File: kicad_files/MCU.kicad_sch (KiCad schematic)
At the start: 24 parts, among them SW1 SW_Push, SW2 SW_Push, U1 STM32F407VGTx, Y1 LFXTAL036869Reel 8MHz Crystal

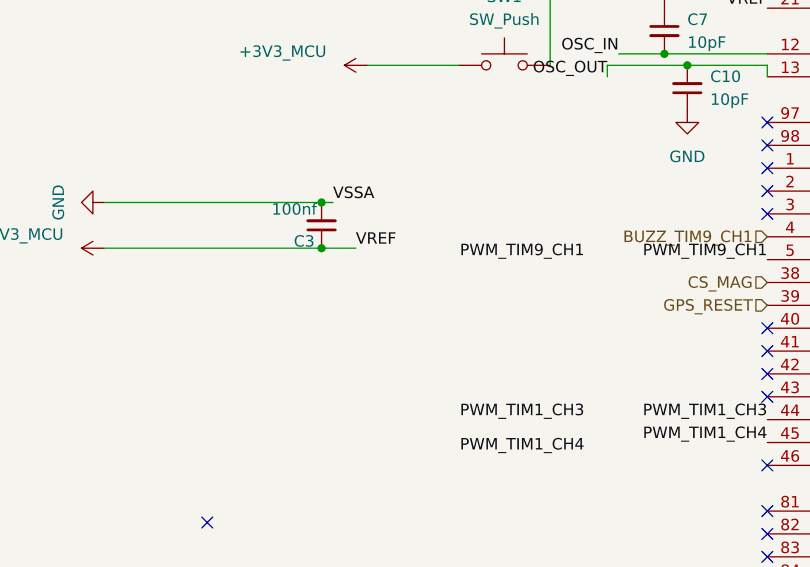
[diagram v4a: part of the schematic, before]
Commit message: add pwm tht hole
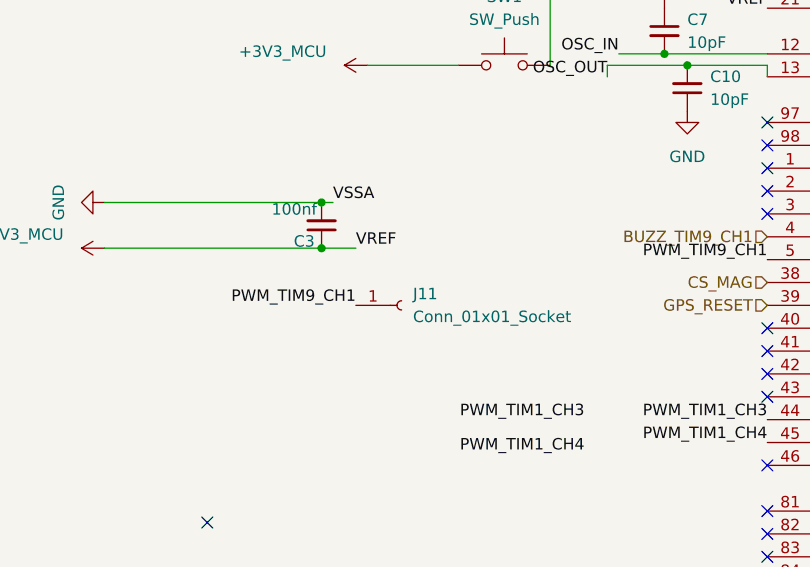
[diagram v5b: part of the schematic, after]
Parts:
- added J11: Conn_01x01_Socket, Connector_Wire:SolderWire-0.5sqmm_1x01_D0.9mm_OD2.1mm, symbol Connector:Conn_01x01_Socket
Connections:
- net PWM_TIM9_CH1: now also J11.1 (Pin_1)
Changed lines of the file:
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@@
 	)
 	(label "PWM_TIM9_CH1"
-		(at 179.07 132.08 180)
+		(at 153.67 137.16 180)
 		(effects
 			(font
@@
 					(unit 1)
 				)
+			)
+		)
+	)
+	(symbol
+		(lib_id "Connector:Conn_01x01_Socket")
+		(at 158.75 137.16 0)
+		(unit 1)
+		(body_style 1)
+		(exclude_from_sim no)
+		(in_bom yes)
+		(on_board yes)
+		(in_pos_files yes)
+		(dnp no)
+		(fields_autoplaced yes)
+		(property "Reference" "J11"
+			(at 160.02 135.8899 0)
+			(show_name no)
+			(do_not_autoplace no)
+			(effects
+				(font
+					(size 1.27 1.27)
+				)
+				(justify left)
+			)
+		)
+		(property "Value" "Conn_01x01_Socket"
+			(at 160.02 138.4299 0)
+			(show_name no)
+			(do_not_autoplace no)
+			(effects
+				(font
+					(size 1.27 1.27)
+				)
+				(justify left)
+			)
+		)
+		(property "Footprint" "Connector_Wire:SolderWire-0.5sqmm_1x01_D0.9mm_OD2.1mm"
+			(at 158.75 137.16 0)
+			(hide yes)
+			(show_name no)
+			(do_not_autoplace no)
+			(effects
+				(font
+					(size 1.27 1.27)
+				)
+			)
+		)
+		(property "Datasheet" ""
+			(at 158.75 137.16 0)
+			(hide yes)
+			(show_name no)
+			(do_not_autoplace no)
+			(effects
+				(font
+					(size 1.27 1.27)
+				)
+			)
+		)
+		(property "Description" "Generic connector, single row, 01x01, script generated"
+			(at 158.75 137.16 0)
+			(hide yes)
+			(show_name no)
+			(do_not_autoplace no)
+			(effects
+				(font
+					(size 1.27 1.27)
+				)
+			)
+		)
+		(pin "1"
+		)
+		(instances
+			(project "versorlite"
+				(path "/1a230af0-0a74-48f7-8607-b087121dda49/a6e36be3-aff5-4566-a903-d81edfd88a96"
+					(reference "J11")
+					(unit 1)
+				)

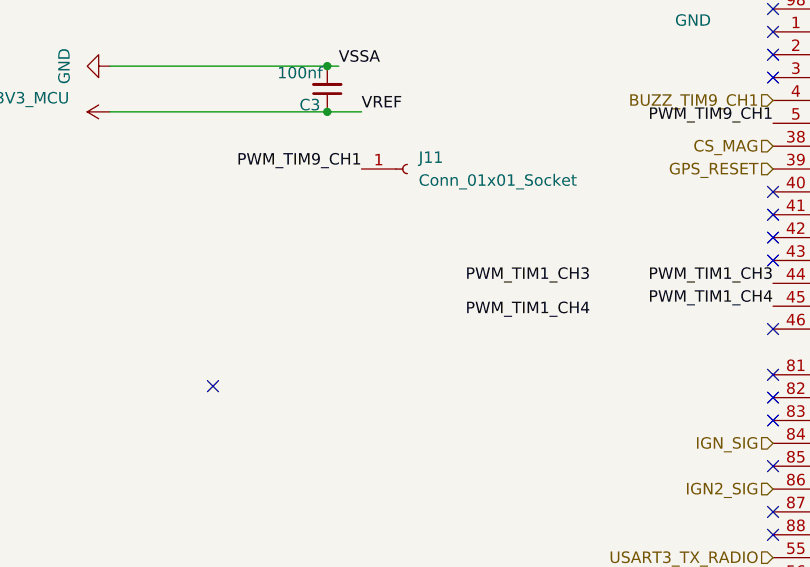
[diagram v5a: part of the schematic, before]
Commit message: add two more pwm holes
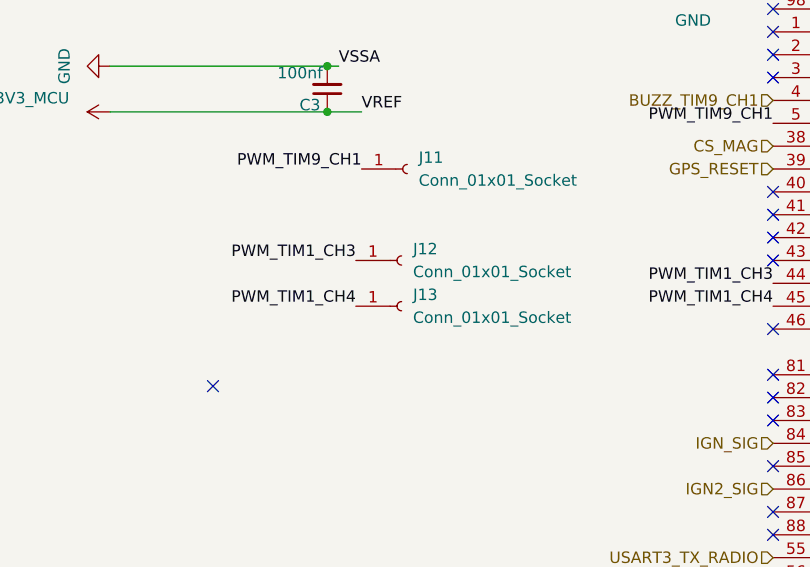
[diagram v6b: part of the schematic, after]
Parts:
- added J12, J13: Conn_01x01_Socket, Connector_Wire:SolderWire-0.5sqmm_1x01_D0.9mm_OD2.1mm, symbol Connector:Conn_01x01_Socket
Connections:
- net PWM_TIM1_CH3: now also J12.1 (Pin_1)
- net PWM_TIM1_CH4: now also J13.1 (Pin_1)
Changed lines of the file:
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@@
 	)
 	(label "PWM_TIM1_CH3"
-		(at 179.07 149.86 180)
+		(at 153.035 147.32 180)
 		(effects
 			(font
@@
 	)
 	(label "PWM_TIM1_CH4"
-		(at 179.07 153.67 180)
+		(at 153.035 152.4 180)
 		(effects
 			(font
@@
 	)
 	(symbol
+		(lib_id "Connector:Conn_01x01_Socket")
+		(at 158.115 152.4 0)
+		(unit 1)
+		(body_style 1)
+		(exclude_from_sim no)
+		(in_bom yes)
+		(on_board yes)
+		(in_pos_files yes)
+		(dnp no)
+		(fields_autoplaced yes)
+		(property "Reference" "J13"
+			(at 159.385 151.1299 0)
+			(show_name no)
+			(do_not_autoplace no)
+			(effects
+				(font
+					(size 1.27 1.27)
+				)
+				(justify left)
+			)
+		)
+		(property "Value" "Conn_01x01_Socket"
+			(at 159.385 153.6699 0)
+			(show_name no)
+			(do_not_autoplace no)
+			(effects
+				(font
+					(size 1.27 1.27)
+				)
+				(justify left)
+			)
+		)
+		(property "Footprint" "Connector_Wire:SolderWire-0.5sqmm_1x01_D0.9mm_OD2.1mm"
+			(at 158.115 152.4 0)
+			(hide yes)
+			(show_name no)
+			(do_not_autoplace no)
+			(effects
+				(font
+					(size 1.27 1.27)
+				)
+			)
+		)
+		(property "Datasheet" ""
+			(at 158.115 152.4 0)
+			(hide yes)
+			(show_name no)
+			(do_not_autoplace no)
+			(effects
+				(font
+					(size 1.27 1.27)
+				)
+			)
+		)
+		(property "Description" "Generic connector, single row, 01x01, script generated"
+			(at 158.115 152.4 0)
+			(hide yes)
+			(show_name no)
+			(do_not_autoplace no)
+			(effects
+				(font
+					(size 1.27 1.27)
+				)
+			)
+		)
+		(pin "1"
+		)
+		(instances
+			(project "versorlite"
+				(path "/1a230af0-0a74-48f7-8607-b087121dda49/a6e36be3-aff5-4566-a903-d81edfd88a96"
+					(reference "J13")
+					(unit 1)
+				)
+			)
+		)
+	)
+	(symbol
 		(lib_id "Device:C_Small")
 		(at 212.09 63.5 90)
@@
 					(unit 1)
 				)
+			)
+		)
+	)
+	(symbol
+		(lib_id "Connector:Conn_01x01_Socket")
+		(at 158.115 147.32 0)
+		(unit 1)
+		(body_style 1)
+		(exclude_from_sim no)
+		(in_bom yes)
+		(on_board yes)
+		(in_pos_files yes)
+		(dnp no)
+		(fields_autoplaced yes)
+		(property "Reference" "J12"
+			(at 159.385 146.0499 0)
+			(show_name no)
+			(do_not_autoplace no)
+			(effects
+				(font
+					(size 1.27 1.27)
+				)
+				(justify left)
+			)
+		)
+		(property "Value" "Conn_01x01_Socket"
+			(at 159.385 148.5899 0)
+			(show_name no)
+			(do_not_autoplace no)
+			(effects
+				(font
+					(size 1.27 1.27)
+				)
+				(justify left)
+			)
+		)
+		(property "Footprint" "Connector_Wire:SolderWire-0.5sqmm_1x01_D0.9mm_OD2.1mm"
+			(at 158.115 147.32 0)
+			(hide yes)
+			(show_name no)
+			(do_not_autoplace no)
+			(effects
+				(font
+					(size 1.27 1.27)
+				)
+			)
+		)
+		(property "Datasheet" ""
+			(at 158.115 147.32 0)
+			(hide yes)
+			(show_name no)
+			(do_not_autoplace no)
+			(effects
+				(font
+					(size 1.27 1.27)
+				)
+			)
+		)
+		(property "Description" "Generic connector, single row, 01x01, script generated"
+			(at 158.115 147.32 0)
+			(hide yes)
+			(show_name no)
+			(do_not_autoplace no)
+			(effects
+				(font
+					(size 1.27 1.27)
+				)
+			)
+		)
+		(pin "1"
+		)
+		(instances
+			(project "versorlite"
+				(path "/1a230af0-0a74-48f7-8607-b087121dda49/a6e36be3-aff5-4566-a903-d81edfd88a96"
+					(reference "J12")
+					(unit 1)
+				)

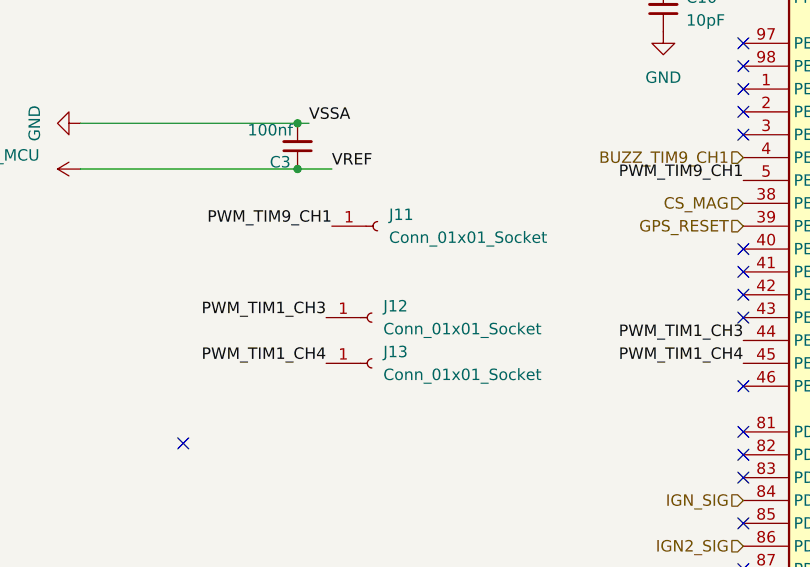
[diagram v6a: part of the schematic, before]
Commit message: size polyfuse, final drc stuff
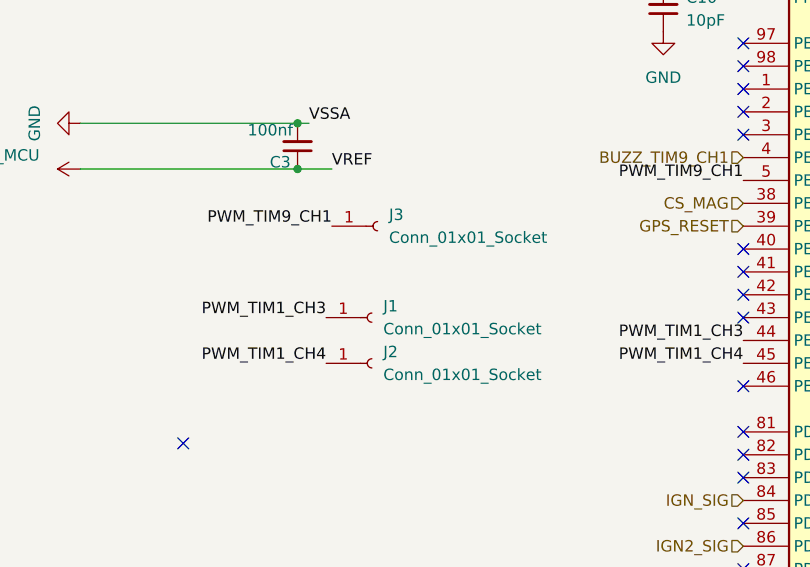
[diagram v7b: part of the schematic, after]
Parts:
- BLM18AG601SZ1D1: footprint Resistor_SMD:R_0603_1608Metric -> Inductor_SMD:L_0603_1608Metric
- renumbered J12 to J1, J13 to J2, J11 to J3
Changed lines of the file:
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@@
 		(dnp no)
 		(fields_autoplaced yes)
-		(property "Reference" "J13"
+		(property "Reference" "J2"
 			(at 159.385 151.1299 0)
 			(show_name no)
@@
 			(project "versorlite"
 				(path "/1a230af0-0a74-48f7-8607-b087121dda49/a6e36be3-aff5-4566-a903-d81edfd88a96"
-					(reference "J13")
+					(reference "J2")
 					(unit 1)
 				)
@@
 			)
 		)
-		(property "Footprint" "Resistor_SMD:R_0603_1608Metric"
+		(property "Footprint" "Inductor_SMD:L_0603_1608Metric"
 			(at 161.29 45.212 90)
 			(hide yes)
@@
 		(dnp no)
 		(fields_autoplaced yes)
-		(property "Reference" "J11"
+		(property "Reference" "J3"
 			(at 160.02 135.8899 0)
 			(show_name no)
@@
 			(project "versorlite"
 				(path "/1a230af0-0a74-48f7-8607-b087121dda49/a6e36be3-aff5-4566-a903-d81edfd88a96"
-					(reference "J11")
+					(reference "J3")
 					(unit 1)
 				)
@@
 		(dnp no)
 		(fields_autoplaced yes)
-		(property "Reference" "J12"
+		(property "Reference" "J1"
 			(at 159.385 146.0499 0)
 			(show_name no)
@@
 			(project "versorlite"
 				(path "/1a230af0-0a74-48f7-8607-b087121dda49/a6e36be3-aff5-4566-a903-d81edfd88a96"
-					(reference "J12")
-					(unit 1)
-				)
+					(reference "J1")
+					(unit 1)
+				)

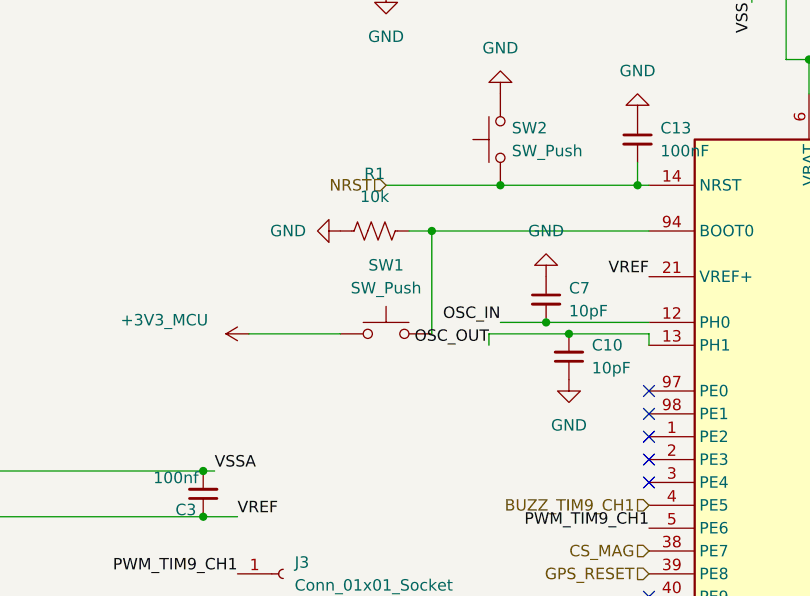
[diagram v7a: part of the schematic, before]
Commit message: better schematic labeling so that mr. dzula isn't confused
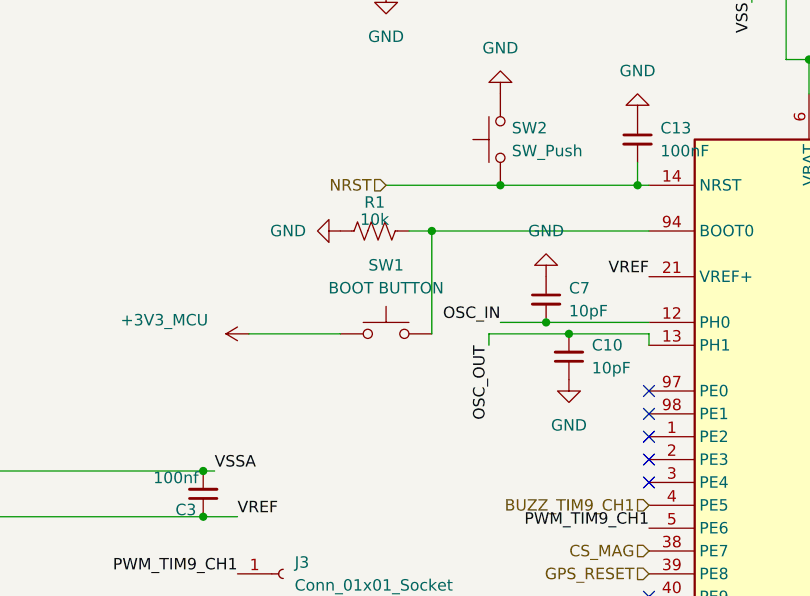
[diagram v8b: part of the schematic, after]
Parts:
- SW1: value SW_Push -> BOOT BUTTON
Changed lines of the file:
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@@
 	)
 	(label "OSC_OUT"
-		(at 181.61 111.76 180)
+		(at 181.61 111.76 270)
 		(effects
 			(font
@@
 			)
 		)
-		(property "Value" "SW_Push"
+		(property "Value" "BOOT BUTTON"
 			(at 170.18 105.41 0)
 			(show_name no)
@@
 		(in_pos_files yes)
 		(dnp no)
-		(fields_autoplaced yes)
 		(property "Reference" "R1"
-			(at 168.91 92.71 90)
+			(at 168.91 95.885 90)
 			(show_name no)
 			(do_not_autoplace no)
@@
 		)
 		(property "Value" "10k"
-			(at 168.91 95.25 90)
-			(show_name no)
-			(do_not_autoplace no)
+			(at 168.91 97.79 90)
+			(show_name no)
+			(do_not_autoplace no)
